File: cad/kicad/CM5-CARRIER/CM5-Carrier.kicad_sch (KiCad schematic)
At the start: 9 parts, among them J101 RAW_POWER_FROM_PWR_SELECT, J102 PWR_STATUS_FROM_SELECTOR, J103 PWR_TELEMETRY_FROM_SELECTOR, J201 AUDIO_TDM_CONTROL, J202 AUDIO_12V_POWER, J401 CPU_FAN, J402 MODEM_FAN, J403 THA0412AD-TZW3_INTAKE, J404 THA0412AD-TZW3_EXHAUST

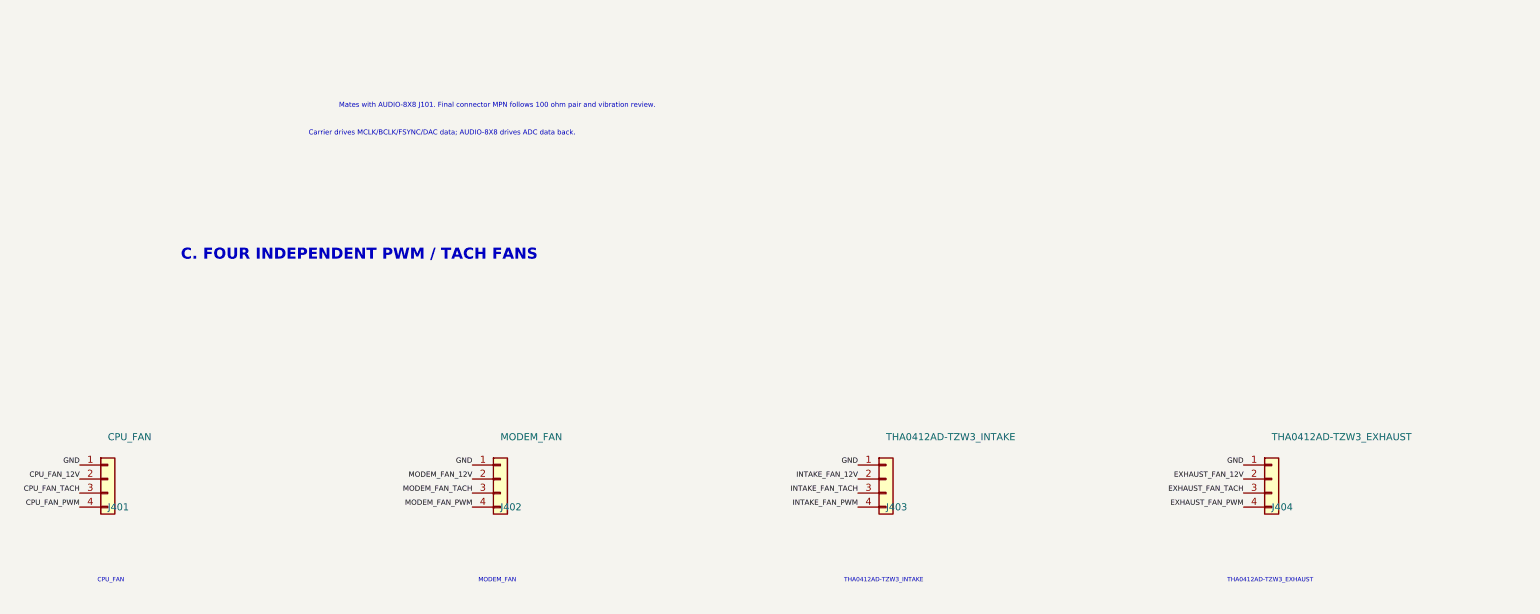
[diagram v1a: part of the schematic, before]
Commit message: Complete A1 detailed carrier and audio capture
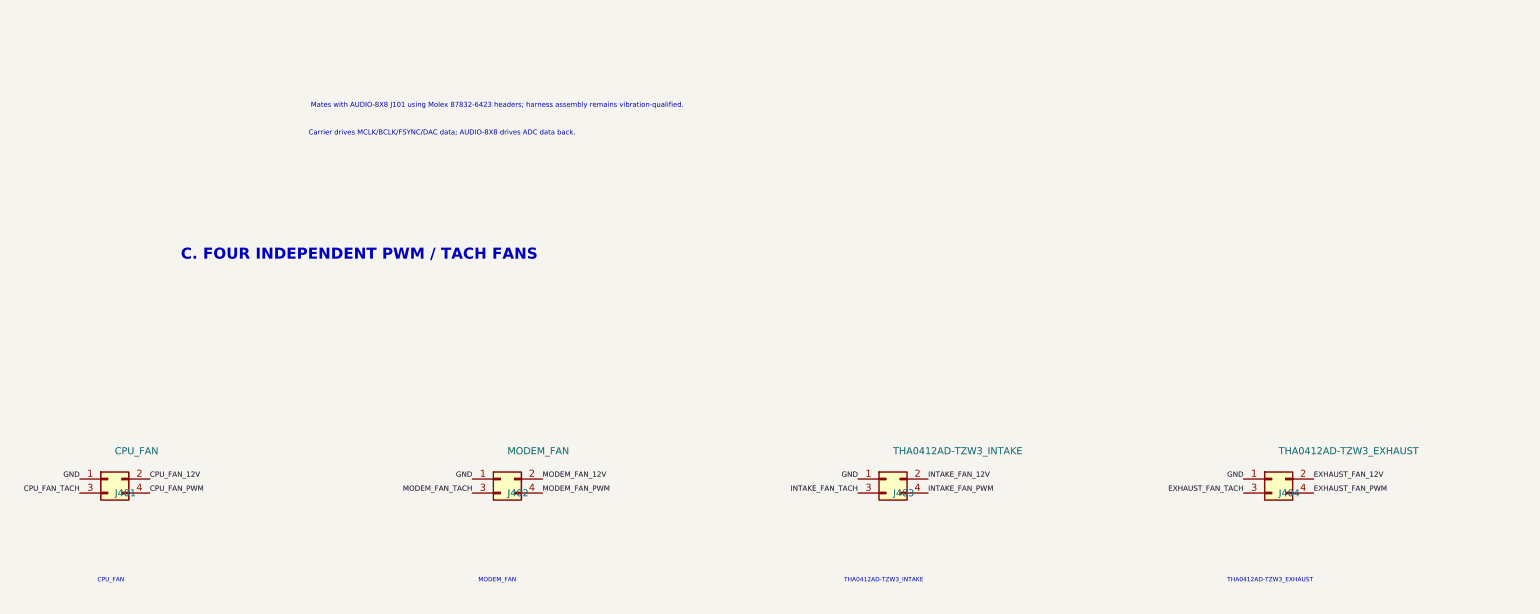
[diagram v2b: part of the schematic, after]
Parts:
- J201: footprint (none) -> Connector_Molex_Milligrid:Molex_8783230xx_2x15_P2.0mm_Header_Vertical_Polarized_MountingPegs; MPN (none) -> 87832-6423; Manufacturer (none) -> Molex
- J401, J402, J403, J404: footprint (none) -> Connector_Molex:Molex_Micro-Fit_3.0_43045-0412_2x02_P3.00mm_Vertical; symbol Connector_Generic:Conn_01x04 -> Connector_Generic:Conn_02x02_Odd_Even; MPN (none) -> 43045-0412; Manufacturer (none) -> Molex
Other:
- note added: "Mates with AUDIO-8X8 J101 using Molex 87832-6423 headers; harness assembly remains vibration-qualified."
- note removed: "Mates with AUDIO-8X8 J101. Final connector MPN follows 100 ohm pair and vibration review."
- moved on the sheet: J401, J402, J403, J404
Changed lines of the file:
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@@
+			)
+		)
+		(property "Footprint" "Connector_Molex_Milligrid:Molex_8783230xx_2x15_P2.0mm_Header_Vertical_Polarized_MountingPegs"
+			(at 69.85 160.02 0.0000)
+			(effects
+				(font
+					(size 1.27 1.27)
+				)
+				(hide yes)
+			)
+		)
+		(property "Manufacturer" "Molex"
+			(at 72.39 165.0999 0)
+			(effects
+				(font
+					(size 1.27 1.27)
+				)
+				(hide yes)
+			)
+		)
+		(property "MPN" "87832-6423"
+			(at 72.39 165.0999 0)
+			(effects
+				(font
+					(size 1.27 1.27)
+				)
+				(hide yes)
 			)
 		)
@@
 	)
 	(symbol
-		(lib_id "Connector_Generic:Conn_01x04")
+		(lib_id "Connector_Generic:Conn_02x02_Odd_Even")
 		(at 44.45 275.59 0)
 		(unit 1)
@@
 		(fields_autoplaced no)
 		(property "Reference" "J401"
-			(at 44.45 280.67 0.0000)
+			(at 45.72 278.13 0.0000)
 			(effects
 				(font
@@
 		)
 		(property "Value" "CPU_FAN"
-			(at 44.45 267.97 0.0000)
+			(at 45.72 270.51 0.0000)
 			(effects
 				(font
@@
 				)
 				(justify left)
+			)
+		)
+		(property "Footprint" "Connector_Molex:Molex_Micro-Fit_3.0_43045-0412_2x02_P3.00mm_Vertical"
+			(at 44.45 275.59 0.0000)
+			(effects
+				(font
+					(size 1.27 1.27)
+				)
+				(hide yes)
+			)
+		)
+		(property "Manufacturer" "Molex"
+			(at 46.99 280.6699 0)
+			(effects
+				(font
+					(size 1.27 1.27)
+				)
+				(hide yes)
+			)
+		)
+		(property "MPN" "43045-0412"
+			(at 46.99 280.6699 0)
+			(effects
+				(font
+					(size 1.27 1.27)
+				)
+				(hide yes)
 			)
 		)
@@
 	)
 	(symbol
-		(lib_id "Connector_Generic:Conn_01x04")
+		(lib_id "Connector_Generic:Conn_02x02_Odd_Even")
 		(at 115.57 275.59 0)
 		(unit 1)
@@
 		(fields_autoplaced no)
 		(property "Reference" "J402"
-			(at 115.57 280.67 0.0000)
+			(at 116.84 278.13 0.0000)
 			(effects
 				(font
@@
 		)
 		(property "Value" "MODEM_FAN"
-			(at 115.57 267.97 0.0000)
+			(at 116.84 270.51 0.0000)
 			(effects
 				(font
@@
 				)
 				(justify left)
+			)
+		)
+		(property "Footprint" "Connector_Molex:Molex_Micro-Fit_3.0_43045-0412_2x02_P3.00mm_Vertical"
+			(at 115.57 275.59 0.0000)
+			(effects
+				(font
+					(size 1.27 1.27)
+				)
+				(hide yes)
+			)
+		)
+		(property "Manufacturer" "Molex"
+			(at 118.11 280.6699 0)
+			(effects
+				(font
+					(size 1.27 1.27)
+				)
+				(hide yes)
+			)
+		)
+		(property "MPN" "43045-0412"
+			(at 118.11 280.6699 0)
+			(effects
+				(font
+					(size 1.27 1.27)
+				)
+				(hide yes)
 			)
 		)
@@
 	)
 	(symbol
-		(lib_id "Connector_Generic:Conn_01x04")
+		(lib_id "Connector_Generic:Conn_02x02_Odd_Even")
 		(at 185.42 275.59 0)
 		(unit 1)
@@
 		(fields_autoplaced no)
 		(property "Reference" "J403"
-			(at 185.42 280.67 0.0000)
+			(at 186.69 278.13 0.0000)
 			(effects
 				(font
@@
 		)
 		(property "Value" "THA0412AD-TZW3_INTAKE"
-			(at 185.42 267.97 0.0000)
+			(at 186.69 270.51 0.0000)
 			(effects
 				(font
@@
 				)
 				(justify left)
+			)
+		)
+		(property "Footprint" "Connector_Molex:Molex_Micro-Fit_3.0_43045-0412_2x02_P3.00mm_Vertical"
+			(at 185.42 275.59 0.0000)
+			(effects
+				(font
+					(size 1.27 1.27)
+				)
+				(hide yes)
+			)
+		)
+		(property "Manufacturer" "Molex"
+			(at 187.96 280.6699 0)
+			(effects
+				(font
+					(size 1.27 1.27)
+				)
+				(hide yes)
+			)
+		)
+		(property "MPN" "43045-0412"
+			(at 187.96 280.6699 0)
+			(effects
+				(font
+					(size 1.27 1.27)
+				)
+				(hide yes)
 			)
 		)
@@
 	)
 	(symbol
-		(lib_id "Connector_Generic:Conn_01x04")
+		(lib_id "Connector_Generic:Conn_02x02_Odd_Even")
 		(at 255.27 275.59 0)
 		(unit 1)
@@
 		(fields_autoplaced no)
 		(property "Reference" "J404"
-			(at 255.27 280.67 0.0000)
+			(at 256.54 278.13 0.0000)
 			(effects
 				(font
@@
 		)
 		(property "Value" "THA0412AD-TZW3_EXHAUST"
-			(at 255.27 267.97 0.0000)
+			(at 256.54 270.51 0.0000)
 			(effects
 				(font
@@
 				)
 				(justify left)
+			)
+		)
+		(property "Footprint" "Connector_Molex:Molex_Micro-Fit_3.0_43045-0412_2x02_P3.00mm_Vertical"
+			(at 255.27 275.59 0.0000)
+			(effects
+				(font
+					(size 1.27 1.27)
+				)
+				(hide yes)
+			)
+		)
+		(property "Manufacturer" "Molex"
+			(at 257.81 280.6699 0)
+			(effects
+				(font
+					(size 1.27 1.27)
+				)
+				(hide yes)
+			)
+		)
+		(property "MPN" "43045-0412"
+			(at 257.81 280.6699 0)
+			(effects
+				(font
+					(size 1.27 1.27)
+				)
+				(hide yes)
 			)
 		)
@@
 	)
 	(label "GND"
-		(at 39.37 273.05 0.0000)
+		(at 39.37 275.59 0.0000)
 		(effects
 			(font
@@
 	)
 	(label "CPU_FAN_12V"
-		(at 39.37 275.59 0.0000)
-		(effects
-			(font
-				(size 0.95 0.95)
-			)
-			(justify right bottom)
+		(at 52.07 275.59 0.0000)
+		(effects
+			(font
+				(size 0.95 0.95)
+			)
+			(justify left bottom)
 		)
 	)
@@
 	)
 	(label "CPU_FAN_PWM"
-		(at 39.37 280.67 0.0000)
-		(effects
-			(font
-				(size 0.95 0.95)
-			)
-			(justify right bottom)
-		)
-	)
-	(label "GND"
-		(at 110.49 273.05 0.0000)
+		(at 52.07 278.13 0.0000)
+		(effects
+			(font
+				(size 0.95 0.95)
+			)
+			(justify left bottom)
+		)
+	)
+	(label "GND"
+		(at 110.49 275.59 0.0000)
 		(effects
 			(font
@@
 	)
 	(label "MODEM_FAN_12V"
-		(at 110.49 275.59 0.0000)
-		(effects
-			(font
-				(size 0.95 0.95)
-			)
-			(justify right bottom)
+		(at 123.19 275.59 0.0000)
+		(effects
+			(font
+				(size 0.95 0.95)
+			)
+			(justify left bottom)
 		)
 	)
@@
 	)
 	(label "MODEM_FAN_PWM"
-		(at 110.49 280.67 0.0000)
-		(effects
-			(font
-				(size 0.95 0.95)
-			)
-			(justify right bottom)
-		)
-	)
-	(label "GND"
-		(at 180.34 273.05 0.0000)
+		(at 123.19 278.13 0.0000)
+		(effects
+			(font
+				(size 0.95 0.95)
+			)
+			(justify left bottom)
+		)
+	)
+	(label "GND"
+		(at 180.34 275.59 0.0000)
 		(effects
 			(font
@@
 	)
 	(label "INTAKE_FAN_12V"
-		(at 180.34 275.59 0.0000)
-		(effects
-			(font
-				(size 0.95 0.95)
-			)
-			(justify right bottom)
+		(at 193.04 275.59 0.0000)
+		(effects
+			(font
+				(size 0.95 0.95)
+			)
+			(justify left bottom)
 		)
 	)
@@
 	)
 	(label "INTAKE_FAN_PWM"
-		(at 180.34 280.67 0.0000)
-		(effects
-			(font
-				(size 0.95 0.95)
-			)
-			(justify right bottom)
-		)
-	)
-	(label "GND"
-		(at 250.19 273.05 0.0000)
+		(at 193.04 278.13 0.0000)
+		(effects
+			(font
+				(size 0.95 0.95)
+			)
+			(justify left bottom)
+		)
+	)
+	(label "GND"
+		(at 250.19 275.59 0.0000)
 		(effects
 			(font
@@
 	)
 	(label "EXHAUST_FAN_12V"
-		(at 250.19 275.59 0.0000)
-		(effects
-			(font
-				(size 0.95 0.95)
-			)
-			(justify right bottom)
+		(at 262.89 275.59 0.0000)
+		(effects
+			(font
+				(size 0.95 0.95)
+			)
+			(justify left bottom)
 		)
 	)
@@
 	)
 	(label "EXHAUST_FAN_PWM"
-		(at 250.19 280.67 0.0000)
-		(effects
-			(font
-				(size 0.95 0.95)
-			)
-			(justify right bottom)
+		(at 262.89 278.13 0.0000)
+		(effects
+			(font
+				(size 0.95 0.95)
+			)
+			(justify left bottom)
 		)
 	)
@@
 		)
 	)
-	(text "Mates with AUDIO-8X8 J101. Final connector MPN follows 100 ohm pair and vibration review."
+	(text "Mates with AUDIO-8X8 J101 using Molex 87832-6423 headers; harness assembly remains vibration-qualified."
 		(exclude_from_sim no)
 		(at 115 208 0.0000)

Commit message: Audit schematic logic against controlled datasheets
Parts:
- J101, J201, J401, J402, J403, J404: now left out of the parts list
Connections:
- net AUD_DAC_MUTE_N renamed AUD_DAC_MUTE_CMD_N
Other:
- added sheet Audio Control / Headset (Audio-Control.kicad_sch)
- added sheet CM5 Core / Allocated Pins (CM5-Core-Allocated.kicad_sch)
- added sheet Display Harness (Display-Harness.kicad_sch)
- added sheet Network / PCIe / Wi-Fi (Network-PCIe.kicad_sch)
- added sheet Power Regulators (Power-Regulators-A1.kicad_sch)
- added sheet Thermal / Fans / IO (Thermal-IO.kicad_sch)
- added sheet WWAN / Dual SIM (WWAN-SIM.kicad_sch)
- note added: "01 CM5-Core-Allocated: exact 300-contact CM5 symbol, 76 owned contacts (74 connected, 2 assigned NC)"
- note added: "11 Review: all three board roots have zero ERC violations; child context is allowlisted"
- note added: "E. CONNECTED CM5-CARRIER HIERARCHY"
- note added: "J101/J201/J401-J404 are interface-only duplicates; the detailed-page connectors own the board footprints."
- note removed: "01 CM5-Core-Allocated: exact 300-contact CM5 symbol, 76 locked functions"
- note removed: "11 Review: every detailed sheet has zero ERC errors; warnings are classified"
